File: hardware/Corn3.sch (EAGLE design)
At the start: 74 parts, among them IC1 STM32F10XCXT6, J1 JTAG-MINI, J4 PICOBLADE-UART-PORT, U3 AS1362, U4 DRV8301

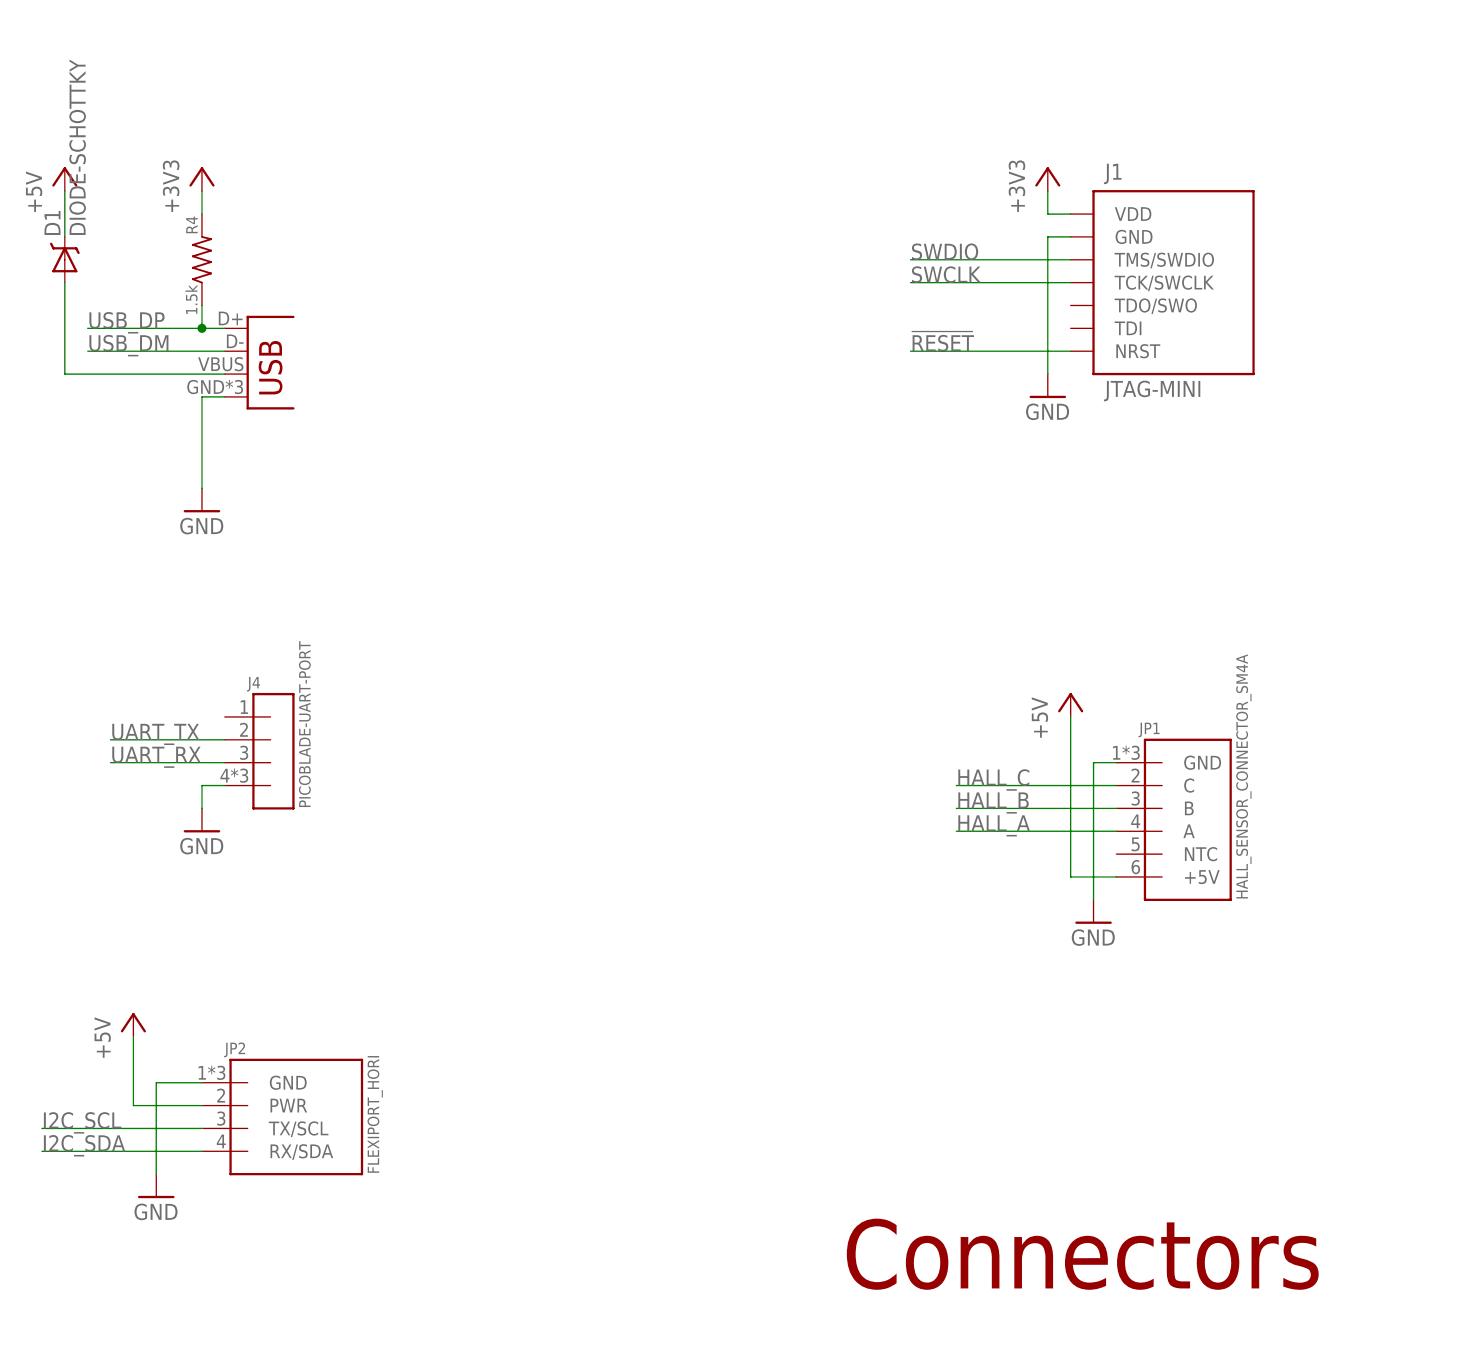
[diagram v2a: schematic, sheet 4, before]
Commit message: Fix reversed Hall connector (#31) and change pinout for flex port.
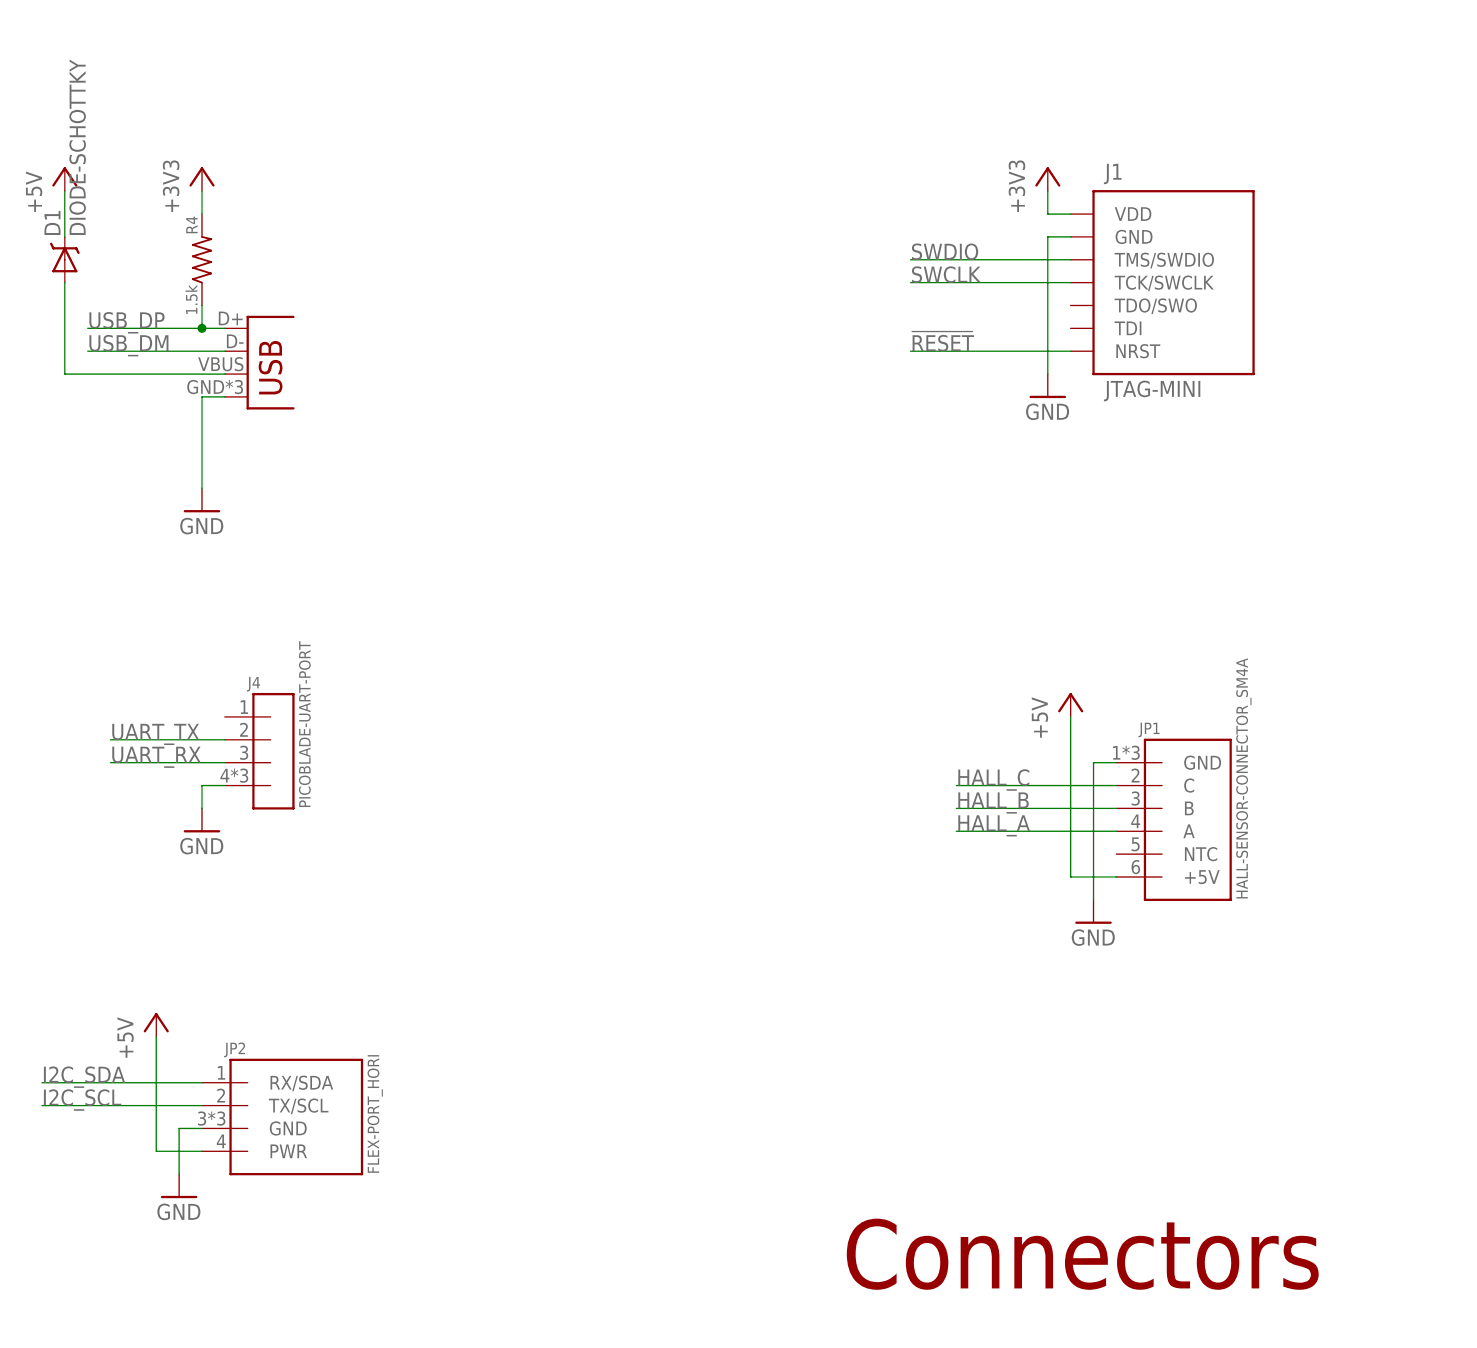
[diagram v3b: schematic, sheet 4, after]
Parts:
- JP1: value HALL_SENSOR_CONNECTOR_SM4A -> HALL-SENSOR-CONNECTOR_SM4A; device Xo-Connector:HALL_SENSOR_CONNECTOR_SM4A -> Xo-Connector:HALL-SENSOR-CONNECTOR_SM4A
- JP2: value FLEXIPORT_HORI -> FLEX-PORT_HORI; device Xo-Connector:FLEXIPORT_HORI -> Xo-Connector:FLEX-PORT_HORI
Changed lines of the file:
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@@
 <part name="R22" library="dan-rcl" deviceset="R" device="0603" value="10k"/>
 <part name="C23" library="dan-rcl" deviceset="C" device="1206" value="4.7uF/50V"/>
-<part name="JP1" library="Xo-Connector" deviceset="HALL_SENSOR_CONNECTOR" device="_SM4A"/>
+<part name="JP1" library="Xo-Connector" deviceset="HALL-SENSOR-CONNECTOR" device="_SM4A"/>
 <part name="P+7" library="supply1" deviceset="V+" device=""/>
 <part name="P-4" library="supply1" deviceset="V-" device=""/>
-<part name="JP2" library="Xo-Connector" deviceset="FLEXIPORT" device="_HORI"/>
+<part name="JP2" library="Xo-Connector" deviceset="FLEX-PORT" device="_HORI"/>
 <part name="C17" library="dan-rcl" deviceset="C" device="0603" value="1uF"/>
 </parts>
@@
 <instance part="VDD4" gate="G$1" x="78.74" y="149.86"/>
 <instance part="R4" gate="G$1" x="78.74" y="139.7" rot="R90"/>
-<instance part="GND15" gate="1" x="73.66" y="35.56"/>
-<instance part="P+6" gate="1" x="71.12" y="55.88"/>
+<instance part="GND15" gate="1" x="76.2" y="35.56"/>
+<instance part="P+6" gate="1" x="73.66" y="55.88"/>
 <instance part="JP3" gate="G$1" x="83.82" y="124.46"/>
 <instance part="D1" gate="G$1" x="63.5" y="139.7" rot="R90"/>
@@
 </segment>
 <segment>
-<pinref part="GND18" gate="1" pin="GND"/>
-<wire x1="177.8" y1="83.82" x2="177.8" y2="68.58" width="0.1524" layer="91"/>
-<pinref part="JP1" gate="G$1" pin="GND"/>
-<wire x1="177.8" y1="83.82" x2="180.34" y2="83.82" width="0.1524" layer="91"/>
-</segment>
-<segment>
 <pinref part="J4" gate="G$1" pin="4"/>
 <pinref part="GND19" gate="1" pin="GND"/>
@@
 <segment>
 <pinref part="GND15" gate="1" pin="GND"/>
-<wire x1="78.74" y1="48.26" x2="73.66" y2="48.26" width="0.1524" layer="91"/>
-<wire x1="73.66" y1="48.26" x2="73.66" y2="38.1" width="0.1524" layer="91"/>
+<wire x1="76.2" y1="43.18" x2="76.2" y2="38.1" width="0.1524" layer="91"/>
 <pinref part="JP2" gate="G$1" pin="GND"/>
+<wire x1="78.74" y1="43.18" x2="76.2" y2="43.18" width="0.1524" layer="91"/>
+</segment>
+<segment>
+<pinref part="JP1" gate="G$1" pin="GND"/>
+<pinref part="JP1" gate="G$1" pin="GND"/>
+<pinref part="GND18" gate="1" pin="GND"/>
+<wire x1="177.8" y1="68.58" x2="177.8" y2="83.82" width="0.1524" layer="91"/>
+<wire x1="177.8" y1="83.82" x2="180.34" y2="83.82" width="0.1524" layer="91"/>
 </segment>
 </net>
@@
 <wire x1="175.26" y1="71.12" x2="175.26" y2="88.9" width="0.1524" layer="91"/>
 <pinref part="JP1" gate="G$1" pin="+5V"/>
+<pinref part="JP1" gate="G$1" pin="+5V"/>
 <wire x1="175.26" y1="71.12" x2="180.34" y2="71.12" width="0.1524" layer="91"/>
 </segment>
 <segment>
 <pinref part="P+6" gate="1" pin="+5V"/>
-<wire x1="78.74" y1="45.72" x2="71.12" y2="45.72" width="0.1524" layer="91"/>
-<wire x1="71.12" y1="45.72" x2="71.12" y2="53.34" width="0.1524" layer="91"/>
+<wire x1="73.66" y1="40.64" x2="73.66" y2="53.34" width="0.1524" layer="91"/>
 <pinref part="JP2" gate="G$1" pin="PWR"/>
+<wire x1="78.74" y1="40.64" x2="73.66" y2="40.64" width="0.1524" layer="91"/>
 </segment>
 <segment>
@@
 <label x="162.56" y="76.2" size="1.778" layer="95"/>
 <pinref part="JP1" gate="G$1" pin="A"/>
+<pinref part="JP1" gate="G$1" pin="A"/>
 </segment>
 </net>
@@
 <label x="162.56" y="78.74" size="1.778" layer="95"/>
 <pinref part="JP1" gate="G$1" pin="B"/>
+<pinref part="JP1" gate="G$1" pin="B"/>
 </segment>
 </net>
@@
 <wire x1="162.56" y1="81.28" x2="180.34" y2="81.28" width="0.1524" layer="91"/>
 <label x="162.56" y="81.28" size="1.778" layer="95"/>
+<pinref part="JP1" gate="G$1" pin="C"/>
 <pinref part="JP1" gate="G$1" pin="C"/>
 </segment>
@@
 <net name="I2C_SDA" class="0">
 <segment>
-<wire x1="60.96" y1="40.64" x2="78.74" y2="40.64" width="0.1524" layer="91"/>
-<label x="60.96" y="40.64" size="1.778" layer="95"/>
+<wire x1="60.96" y1="48.26" x2="78.74" y2="48.26" width="0.1524" layer="91"/>
+<label x="60.96" y="48.26" size="1.778" layer="95"/>
 <pinref part="JP2" gate="G$1" pin="RX/SDA"/>
 </segment>
@@
 <net name="I2C_SCL" class="0">
 <segment>
-<wire x1="60.96" y1="43.18" x2="78.74" y2="43.18" width="0.1524" layer="91"/>
-<label x="60.96" y="43.18" size="1.778" layer="95"/>
+<wire x1="60.96" y1="45.72" x2="78.74" y2="45.72" width="0.1524" layer="91"/>
+<label x="60.96" y="45.72" size="1.778" layer="95"/>
 <pinref part="JP2" gate="G$1" pin="TX/SCL"/>
 </segment>
